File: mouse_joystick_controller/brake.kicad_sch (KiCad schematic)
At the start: 5 parts, among them Q1 MOSFET-N-CH, Q2 MOSFET-P-CH-EN-BUK6D120-60PX

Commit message: Modify brake
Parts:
- removed Q2: MOSFET-P-CH-EN-BUK6D120-60PX, Janelia:DFN2020-MD6-MOSFET, symbol Janelia:MOSFET-P-CH-EN-BUK6D120-60PX
- removed R3 (x2): 1k, Janelia:R_0402_1005Metric, symbol Janelia:R_1k_0402
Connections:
- net POWER_ENABLE is gone; now on net BRAKE_PWM: R3.1
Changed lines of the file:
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@@
     (company "Howard Hughes Medical Institute")
   )
-  (junction (at 142.24 90.17) (diameter 0) (color 0 0 0 0)
-  )
-  (wire (pts (xy 139.7 90.17) (xy 142.24 90.17))
+  (wire (pts (xy 76.2 92.71) (xy 73.66 92.71))
     (stroke (width 0) (type default))
   )
-  (wire (pts (xy 142.24 87.63) (xy 142.24 90.17))
+  (wire (pts (xy 76.2 96.52) (xy 73.66 96.52))
     (stroke (width 0) (type default))
   )
-  (wire (pts (xy 165.1 81.28) (xy 165.1 83.82))
-    (stroke (width 0) (type default))
-  )
-  (wire (pts (xy 172.72 88.9) (xy 175.26 88.9))
-    (stroke (width 0) (type default))
-  )
-  (wire (pts (xy 142.24 72.39) (xy 142.24 74.93))
+  (wire (pts (xy 76.2 88.9) (xy 73.66 88.9))
     (stroke (width 0) (type default))
   )
@@
     (stroke (width 0) (type default))
   )
-  (wire (pts (xy 142.24 107.95) (xy 142.24 105.41))
-    (stroke (width 0) (type default))
-  )
-  (wire (pts (xy 142.24 90.17) (xy 142.24 92.71))
-    (stroke (width 0) (type default))
-  )
   (wire (pts (xy 110.49 124.46) (xy 110.49 127))
-    (stroke (width 0) (type default))
-  )
-  (wire (pts (xy 165.1 96.52) (xy 165.1 93.98))
     (stroke (width 0) (type default))
   )
@@
     (effects (font (size 1.27 1.27)) (justify right bottom))
   )
-  (label "+24V" (at 165.1 96.52 270) (fields_autoplaced)
-    (effects (font (size 1.27 1.27)) (justify right bottom))
-  )
   (label "GND" (at 110.49 127 270) (fields_autoplaced)
     (effects (font (size 1.27 1.27)) (justify right bottom))
   )
-  (label "~{POWER_ENABLE}" (at 175.26 88.9 0) (fields_autoplaced)
+  (label "BRAKE_PWM" (at 110.49 109.22 90) (fields_autoplaced)
     (effects (font (size 1.27 1.27)) (justify left bottom))
   )
-  (label "POWER_ENABLE" (at 110.49 109.22 90) (fields_autoplaced)
+  (label "+24V" (at 76.2 88.9 0) (fields_autoplaced)
     (effects (font (size 1.27 1.27)) (justify left bottom))
   )
-  (label "VAA" (at 142.24 72.39 90) (fields_autoplaced)
+  (label "GND" (at 76.2 92.71 0) (fields_autoplaced)
     (effects (font (size 1.27 1.27)) (justify left bottom))
   )
-  (label "~{POWER_ENABLE}" (at 139.7 90.17 180) (fields_autoplaced)
-    (effects (font (size 1.27 1.27)) (justify right bottom))
-  )
-  (label "VAA" (at 165.1 81.28 90) (fields_autoplaced)
+  (label "BRAKE_PWM" (at 76.2 96.52 0) (fields_autoplaced)
     (effects (font (size 1.27 1.27)) (justify left bottom))
   )
   (label "BRAKE_PWM" (at 132.08 113.03 180) (fields_autoplaced)
     (effects (font (size 1.27 1.27)) (justify right bottom))
+  )
+  (hierarchical_label "GND" (shape passive) (at 73.66 92.71 180) (fields_autoplaced)
+    (effects (font (size 1.27 1.27)) (justify right))
+  )
+  (hierarchical_label "+24V" (shape passive) (at 73.66 88.9 180) (fields_autoplaced)
+    (effects (font (size 1.27 1.27)) (justify right))
+  )
+  (hierarchical_label "BRAKE_PWM" (shape input) (at 73.66 96.52 180) (fields_autoplaced)
+    (effects (font (size 1.27 1.27)) (justify right))
   )
   (symbol (lib_id "Janelia:MOSFET-N-CH-EN-CSD17483F4") (at 139.7 113.03 0) (unit 1)
@@
         )
       )
-    )
-  )
-  (symbol (lib_id "Janelia:R_1k_0402") (at 142.24 99.06 0) (unit 1)
-    (in_bom yes) (on_board yes) (dnp no)
-    (property "Reference" "R3" (at 144.78 99.06 90)
-      (effects (font (size 1.016 1.016)))
-    )
-    (property "Value" "1k" (at 142.24 99.06 90)
-      (effects (font (size 0.762 0.762)))
-    )
-    (property "Footprint" "Janelia:R_0402_1005Metric" (at 140.462 99.06 90)
-      (effects (font (size 0.762 0.762)) hide)
-    )
-    (property "Datasheet" "" (at 144.272 99.06 90)
-      (effects (font (size 0.762 0.762)))
-    )
-    (property "Vendor" "Digi-Key" (at 146.812 96.52 90)
-      (effects (font (size 1.524 1.524)) hide)
-    )
-    (property "Vendor Part Number" "311-1.00KLRCT-ND" (at 149.352 93.98 90)
-      (effects (font (size 1.524 1.524)) hide)
-    )
-    (property "Description" "RES SMD 1K OHM 1% 1/16W" (at 151.892 91.44 90)
-      (effects (font (size 1.524 1.524)) hide)
-    )
-    (property "Package" "0402" (at 142.24 99.06 0)
-      (effects (font (size 1.27 1.27)) hide)
-    )
-    (property "Manufacturer" "YAGEO" (at 142.24 99.06 0)
-      (effects (font (size 1.27 1.27)) hide)
-    )
-    (property "Manufacturer Part Number" "RC0402FR-071KL" (at 142.24 99.06 0)
-      (effects (font (size 1.27 1.27)) hide)
-    )
-    (pin "1")
-    (pin "2")
-    (instances
-      (project "mouse_joystick_controller"
-        (path "/cc457ebc-4af6-4663-b19f-8cb38f061cb4"
-          (reference "R3") (unit 1)
-        )
-        (path "/cc457ebc-4af6-4663-b19f-8cb38f061cb4/f62b8726-10b6-4dce-a8d7-bdccf22557c3"
-          (reference "R11") (unit 1)
-        )
-        (path "/cc457ebc-4af6-4663-b19f-8cb38f061cb4/588c1a3c-052e-4e39-a8d9-29d79b9f5498"
-          (reference "R11") (unit 1)
-        )
-      )
-    )
-  )
-  (symbol (lib_id "Janelia:R_1k_0402") (at 142.24 81.28 0) (unit 1)
-    (in_bom yes) (on_board yes) (dnp no)
-    (property "Reference" "R3" (at 144.78 81.28 90)
-      (effects (font (size 1.016 1.016)))
-    )
-    (property "Value" "1k" (at 142.24 81.28 90)
-      (effects (font (size 0.762 0.762)))
-    )
-    (property "Footprint" "Janelia:R_0402_1005Metric" (at 140.462 81.28 90)
-      (effects (font (size 0.762 0.762)) hide)
-    )
-    (property "Datasheet" "" (at 144.272 81.28 90)
-      (effects (font (size 0.762 0.762)))
-    )
-    (property "Vendor" "Digi-Key" (at 146.812 78.74 90)
-      (effects (font (size 1.524 1.524)) hide)
-    )
-    (property "Vendor Part Number" "311-1.00KLRCT-ND" (at 149.352 76.2 90)
-      (effects (font (size 1.524 1.524)) hide)
-    )
-    (property "Description" "RES SMD 1K OHM 1% 1/16W" (at 151.892 73.66 90)
-      (effects (font (size 1.524 1.524)) hide)
-    )
-    (property "Package" "0402" (at 142.24 81.28 0)
-      (effects (font (size 1.27 1.27)) hide)
-    )
-    (property "Manufacturer" "YAGEO" (at 142.24 81.28 0)
-      (effects (font (size 1.27 1.27)) hide)
-    )
-    (property "Manufacturer Part Number" "RC0402FR-071KL" (at 142.24 81.28 0)
-      (effects (font (size 1.27 1.27)) hide)
-    )
-    (pin "1")
-    (pin "2")
-    (instances
-      (project "mouse_joystick_controller"
-        (path "/cc457ebc-4af6-4663-b19f-8cb38f061cb4"
-          (reference "R3") (unit 1)
-        )
-        (path "/cc457ebc-4af6-4663-b19f-8cb38f061cb4/f62b8726-10b6-4dce-a8d7-bdccf22557c3"
-          (reference "R10") (unit 1)
-        )
-        (path "/cc457ebc-4af6-4663-b19f-8cb38f061cb4/588c1a3c-052e-4e39-a8d9-29d79b9f5498"
-          (reference "R10") (unit 1)
-        )
-      )
-    )
-  )
-  (symbol (lib_id "Janelia:MOSFET-P-CH-EN-BUK6D120-60PX") (at 167.64 88.9 180) (unit 1)
-    (in_bom yes) (on_board yes) (dnp no)
-    (property "Reference" "Q2" (at 162.56 88.9 0)
-      (effects (font (size 1.27 1.27)) (justify left))
-    )
-    (property "Value" "MOSFET-P-CH-EN-BUK6D120-60PX" (at 161.29 86.995 0)
-      (effects (font (size 1.27 1.27)) (justify left) hide)
-    )
-    (property "Footprint" "Janelia:DFN2020-MD6-MOSFET" (at 177.8 116.84 0)
-      (effects (font (size 1.27 1.27) italic) (justify left) hide)
-    )
-    (property "Datasheet" "" (at 167.64 88.9 0)
-      (effects (font (size 1.27 1.27)) (justify left) hide)
-    )
-    (property "Description" "MOSFET P-CH 60V 3A/8A" (at 167.64 104.14 0)
-      (effects (font (size 1.27 1.27)) hide)
-    )
-    (property "Manufacturer" "Nexperia USA Inc." (at 167.64 101.6 0)
-      (effects (font (size 1.27 1.27)) hide)
-    )
-    (property "Manufacturer Part Number" "BUK6D120-60PX" (at 167.64 111.76 0)
-      (effects (font (size 1.27 1.27)) hide)
-    )
-    (property "Vendor" "Digi-Key" (at 167.64 109.22 0)
-      (effects (font (size 1.27 1.27)) hide)
-    )
-    (property "Vendor Part Number" "1727-8337-1-ND" (at 167.64 106.68 0)
-      (effects (font (size 1.27 1.27)) hide)
-    )
-    (property "Package" "6-UDFN Exposed Pad" (at 167.64 114.3 0)
-      (effects (font (size 1.27 1.27)) hide)
-    )
-    (pin "1")
-    (pin "2")
-    (pin "3")
-    (instances
-      (project "mouse_joystick_controller"
-        (path "/cc457ebc-4af6-4663-b19f-8cb38f061cb4/f62b8726-10b6-4dce-a8d7-bdccf22557c3"
-          (reference "Q2") (unit 1)
-        )
-        (path "/cc457ebc-4af6-4663-b19f-8cb38f061cb4/588c1a3c-052e-4e39-a8d9-29d79b9f5498"
-          (reference "Q2") (unit 1)
-        )
-      )

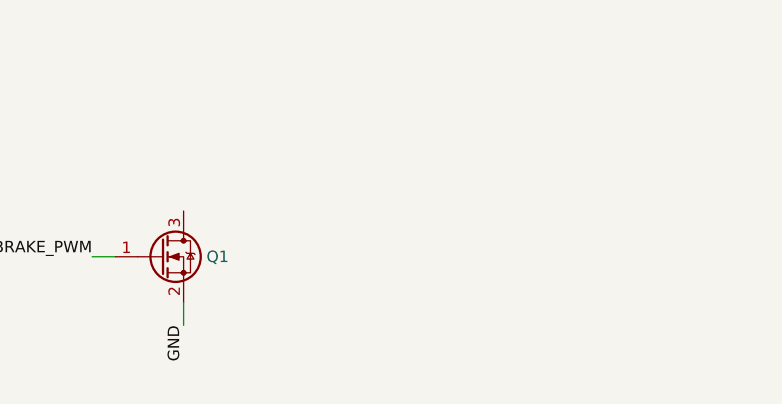
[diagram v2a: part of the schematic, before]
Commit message: Add encoder, lickport, and torque_sensor sheets
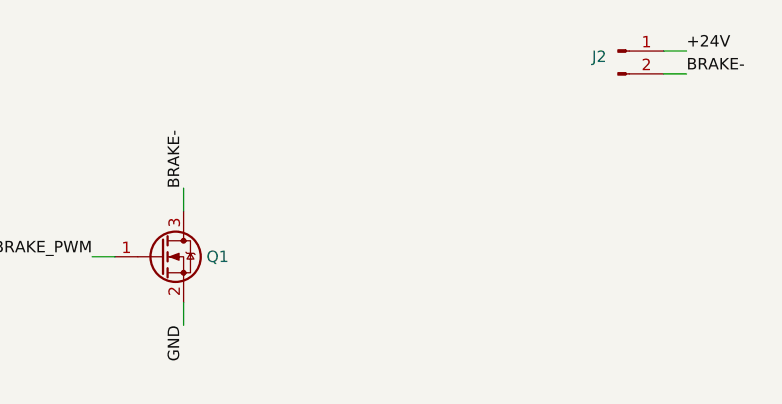
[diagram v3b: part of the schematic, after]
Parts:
- added J2: Conn_TERM_HDR_01x02_Pin_3.5MM_Horizontal, Janelia:TERM_HDR_01x02_Pin_Horizontal_3.5MM_1844210, symbol Janelia:Conn_TERM_HDR_01x02_Pin_3.5MM_Horizontal
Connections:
- net +24V: now also J2.1 (Pin_1)
- net BRAKE-: now reaches Q1.3 (D)
- net BRAKE-: now also J2.2 (Pin_2)
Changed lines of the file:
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@@
   (title_block
     (title "mouse_joystick_controller")
-    (date "2023-05-18")
+    (date "2023-05-22")
     (rev "2.0")
     (company "Howard Hughes Medical Institute")
   )
+  (wire (pts (xy 198.12 92.71) (xy 195.58 92.71))
+    (stroke (width 0) (type default))
+  )
   (wire (pts (xy 76.2 92.71) (xy 73.66 92.71))
     (stroke (width 0) (type default))
@@
     (stroke (width 0) (type default))
   )
+  (wire (pts (xy 198.12 90.17) (xy 195.58 90.17))
+    (stroke (width 0) (type default))
+  )
   (wire (pts (xy 110.49 109.22) (xy 110.49 111.76))
     (stroke (width 0) (type default))
   )
   (wire (pts (xy 142.24 118.11) (xy 142.24 120.65))
+    (stroke (width 0) (type default))
+  )
+  (wire (pts (xy 142.24 105.41) (xy 142.24 107.95))
     (stroke (width 0) (type default))
   )
@@
     (effects (font (size 1.27 1.27)) (justify right bottom))
   )
+  (label "BRAKE-" (at 142.24 105.41 90) (fields_autoplaced)
+    (effects (font (size 1.27 1.27)) (justify left bottom))
+  )
+  (label "+24V" (at 198.12 90.17 0) (fields_autoplaced)
+    (effects (font (size 1.27 1.27)) (justify left bottom))
+  )
   (label "GND" (at 110.49 127 270) (fields_autoplaced)
     (effects (font (size 1.27 1.27)) (justify right bottom))
@@
   (label "BRAKE_PWM" (at 132.08 113.03 180) (fields_autoplaced)
     (effects (font (size 1.27 1.27)) (justify right bottom))
+  )
+  (label "BRAKE-" (at 198.12 92.71 0) (fields_autoplaced)
+    (effects (font (size 1.27 1.27)) (justify left bottom))
   )
   (hierarchical_label "GND" (shape passive) (at 73.66 92.71 180) (fields_autoplaced)
@@
         )
       )
+    )
+  )
+  (symbol (lib_id "Janelia:Conn_TERM_HDR_01x02_Pin_3.5MM_Horizontal") (at 190.5 90.17 0) (unit 1)
+    (in_bom yes) (on_board yes) (dnp no) (fields_autoplaced)
+    (property "Reference" "J2" (at 189.23 90.805 0)
+      (effects (font (size 1.27 1.27)) (justify right))
+    )
+    (property "Value" "Conn_TERM_HDR_01x02_Pin_3.5MM_Horizontal" (at 190.5 102.87 0)
+      (effects (font (size 1.27 1.27)) hide)
+    )
+    (property "Footprint" "Janelia:TERM_HDR_01x02_Pin_Horizontal_3.5MM_1844210" (at 190.5 54.61 0)
+      (effects (font (size 1.27 1.27)) hide)
+    )
+    (property "Datasheet" "" (at 190.5 68.58 0)
+      (effects (font (size 1.27 1.27)) hide)
+    )
+    (property "Manufacturer" "Phoenix Contact" (at 190.5 57.15 0)
+      (effects (font (size 1.27 1.27)) hide)
+    )
+    (property "Manufacturer Part Number" "1844210" (at 190.5 62.23 0)
+      (effects (font (size 1.27 1.27)) hide)
+    )
+    (property "Description" "TERM BLOCK HDR 2POS 90DEG 3.5MM" (at 190.5 64.77 0)
+      (effects (font (size 1.27 1.27)) hide)
+    )
+    (property "Vendor" "Digi-Key" (at 190.5 59.69 0)
+      (effects (font (size 1.27 1.27)) hide)
+    )
+    (property "Vendor Part Number" "277-2416-ND" (at 190.5 67.31 0)
+      (effects (font (size 1.27 1.27)) hide)
+    )
+    (pin "1")
+    (pin "2")
+    (instances
+      (project "mouse_joystick_controller"
+        (path "/cc457ebc-4af6-4663-b19f-8cb38f061cb4/588c1a3c-052e-4e39-a8d9-29d79b9f5498"
+          (reference "J2") (unit 1)
+        )
+      )

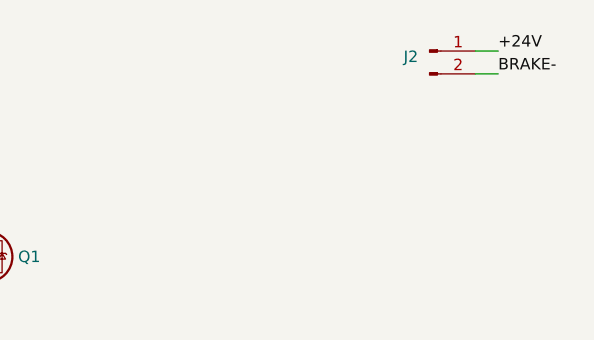
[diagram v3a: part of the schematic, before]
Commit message: Rearrange sheets
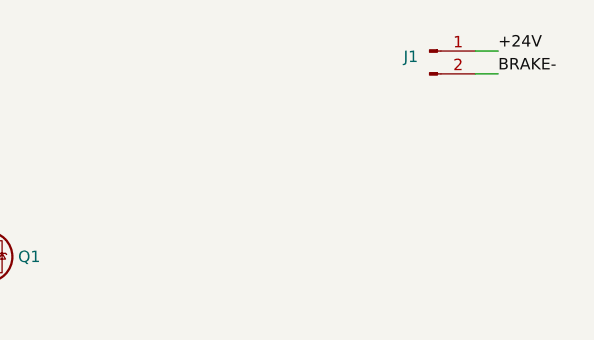
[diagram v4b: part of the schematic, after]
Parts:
- renumbered J2 to J1
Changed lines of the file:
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@@
   (title_block
     (title "mouse_joystick_controller")
-    (date "2023-05-22")
+    (date "2023-05-24")
     (rev "2.0")
     (company "Howard Hughes Medical Institute")
@@
         )
         (path "/cc457ebc-4af6-4663-b19f-8cb38f061cb4/588c1a3c-052e-4e39-a8d9-29d79b9f5498"
-          (reference "R9") (unit 1)
+          (reference "R1") (unit 1)
         )
       )
@@
   (symbol (lib_id "Janelia:Conn_TERM_HDR_01x02_Pin_3.5MM_Horizontal") (at 190.5 90.17 0) (unit 1)
     (in_bom yes) (on_board yes) (dnp no) (fields_autoplaced)
-    (property "Reference" "J2" (at 189.23 90.805 0)
+    (property "Reference" "J1" (at 189.23 90.805 0)
       (effects (font (size 1.27 1.27)) (justify right))
     )
@@
       (project "mouse_joystick_controller"
         (path "/cc457ebc-4af6-4663-b19f-8cb38f061cb4/588c1a3c-052e-4e39-a8d9-29d79b9f5498"
-          (reference "J2") (unit 1)
+          (reference "J1") (unit 1)
         )
       )

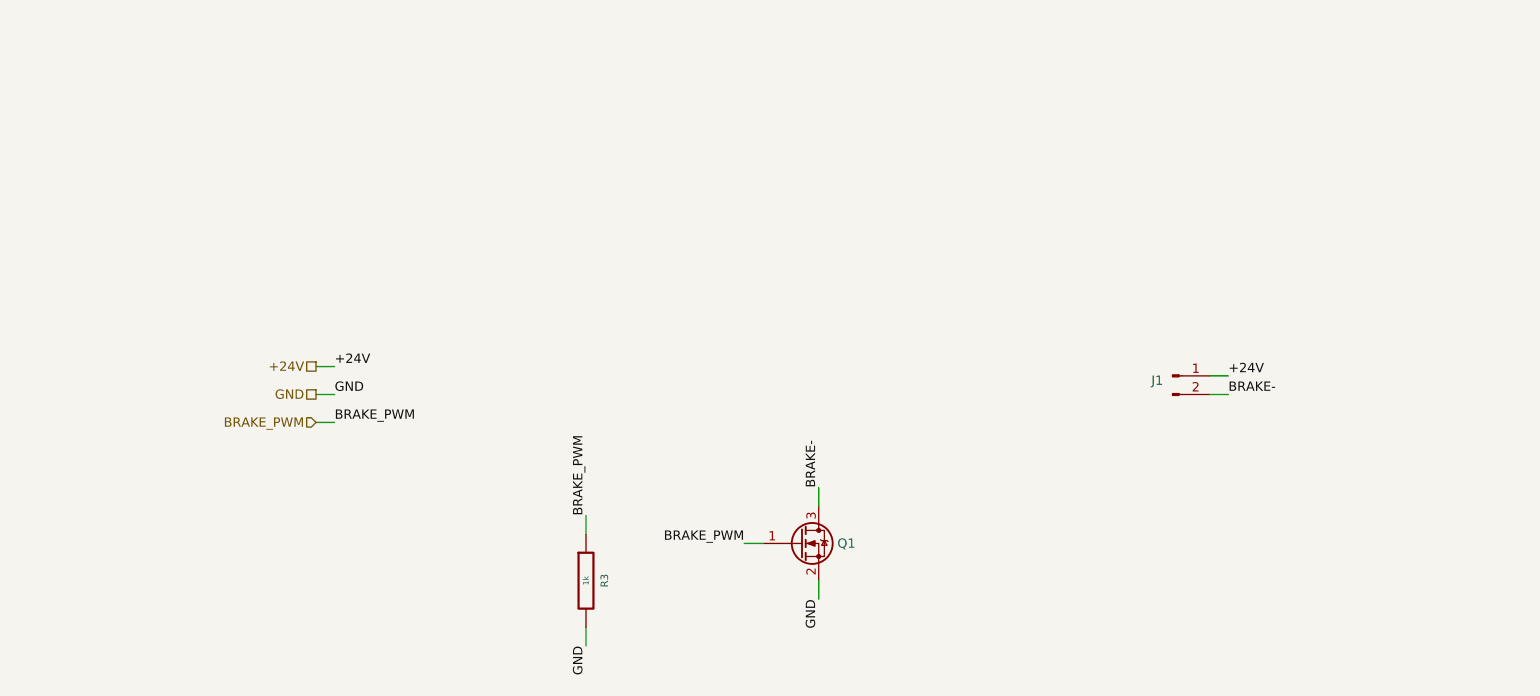
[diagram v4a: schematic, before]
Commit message: Modify brake circuit
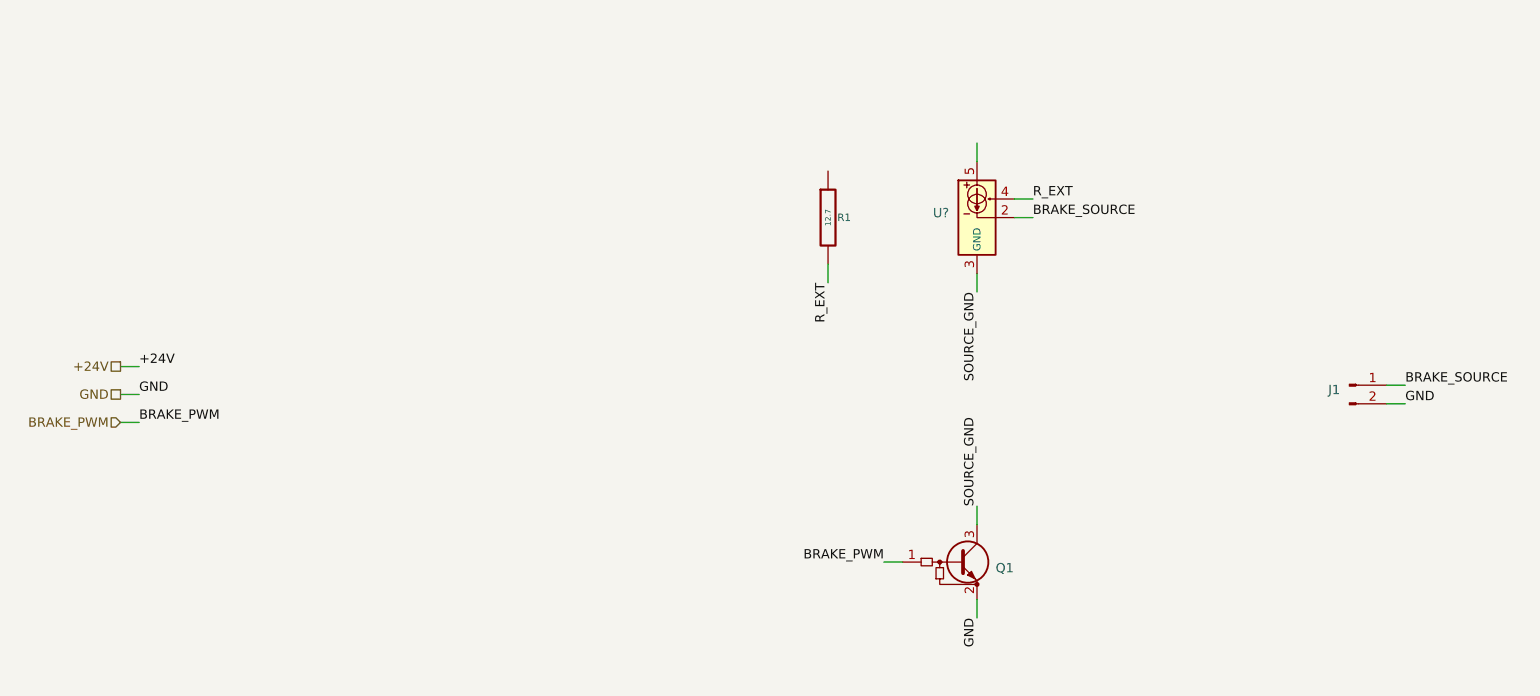
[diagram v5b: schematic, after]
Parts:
- removed Q1: MOSFET-N-CH, Janelia:XFDFN-3, symbol Janelia:MOSFET-N-CH-EN-CSD17483F4
- removed R3: 1k, Janelia:R_0402_1005Metric, symbol Janelia:R_1k_0402
- added Q1: Q_NPN_ECB_BRT, Janelia:XFDFN-3, symbol Janelia:Q_NPN_ECB_BRT_50V_100mA_PDTC124XMB,315
- added R1: 12.7, Janelia:R_0402_1005Metric, symbol Janelia:R_12.7_0402
- added U?: PSSI2021SAY, Janelia:SOT-353_SC-70-5, symbol Janelia:PSSI2021SAY
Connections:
- net BRAKE- is gone; now on net GND: J1.2 (Pin_2)
- net +24V: no longer J1.1 (Pin_1)
- net BRAKE_PWM: now also Q1.1 (B)
- net GND: now also Q1.2 (E)
- new net BRAKE_SOURCE: J1.1 (Pin_1), U?.2
- new net R_EXT: R1.2, U?.4
- new net SOURCE_GND: Q1.3 (C), U?.3 (GND)
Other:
- moved on the sheet: J1
